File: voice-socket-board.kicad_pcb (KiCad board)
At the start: 2 copper layers, 150 x 100 mm, 278 parts, among them J1 JACK_MONO_SW, J2 JACK_MONO_SW, J3 JACK_MONO_SW, P1 CONN_01X03, P2 CONN_01X03, P3 CONN_02X05, P4 DDR3-DIMM, Q1 MMBT3904, Q2 DMMT3904W, Q3 2N7002, Q4 2N7002, Q5 MMBT3904, Q6 2N3906, Q7 MMBT3904, Q8 MMBT3904, Q9 MMBT3904, SW1 SPST, SW10 SP3T, SW11 SP3T, SW12 SP3T, SW13 SP3T, SW14 SPST, SW15 TACT_SWITCH, SW2 SPST, SW3 SP3T, SW4 SP3T, SW5 SPST, SW6 SPST, SW7 Switch_SPDT_x2, SW8 2P3T, SW9 SP3T, U1 LM833, U10 TL072-, U11 NE5534, U2 TL072-, U3 TL072-, U4 TL072-, U5 TL072-, U6 TL072-, U7 MAX9945, U8 CD4013, U9 TL072-

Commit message: routing. tedious
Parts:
- R119: moved to B.Cu
- moved R119 187.1 mm to (165.5, 121.5), turned to 270 degrees
- moved R73 6.19 mm to (140.5, 127.0), turned to 180 degrees
- moved R115 5.59 mm to (162.5, 127.5), turned to 180 degrees
- moved C61 1.50 mm to (159.5, 121.5)
- moved D8 1.00 mm to (158.0, 121.5)
- moved Q8 1.00 mm to (162.5, 124.5), turned to 180 degrees
- moved R72 0.25 mm to (145.5, 122.5)
- turned R117 to 270 degrees
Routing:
- net EG1_GATE: track 0.00 -> 85.4 mm, vias 0 -> 2
- net Net-(R118-Pad1): track 0.00 -> 21.7 mm
- net Net-(Q3-Pad6): track 0.00 -> 19.4 mm, vias 0 -> 2
- net Net-(D5-Pad1): track 0.00 -> 14.9 mm
- net LFO_GATE: track 17.7 -> 32.3 mm
- net Net-(J3-Pad3): track 0.00 -> 14.4 mm
- net Net-(C20-Pad2): track 3.58 -> 14.7 mm
- net Net-(C21-Pad1): track 4.22 -> 14.4 mm
- net Net-(D5-Pad2): track 0.00 -> 9.41 mm, vias 0 -> 2
- net Net-(C19-Pad1): track 0.00 -> 9.13 mm
- net NOISE: track 0.00 -> 8.63 mm
- net Net-(C20-Pad1): track 0.00 -> 7.63 mm
- net Net-(Q7-Pad2): track 0.00 -> 7.14 mm
- net Net-(D3-Pad2): track 0.00 -> 7.09 mm
- net Net-(C18-Pad1): track 0.00 -> 5.97 mm
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
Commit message: routing..........
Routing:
- net Net-(R97-Pad2): track 0.00 -> 65.1 mm
- net Net-(TR1-Pad1): track 3.59 -> 59.7 mm
- net Net-(R98-Pad2): track 0.00 -> 52.8 mm
- net Net-(C57-Pad2): track 9.72 -> 50.7 mm
- net Net-(R100-Pad2): track 0.00 -> 40.2 mm
- net Net-(C62-Pad2): track 0.00 -> 10.6 mm
- net Net-(C62-Pad1): track 0.00 -> 7.53 mm
- net VCO2_PITCH_CV: track 29.6 -> 35.3 mm
- net KEY_TRACK: track 17.2 -> 20.7 mm
- net Net-(J2-Pad3): track 0.00 -> 2.00 mm
- net +12V: track 175.8 -> 177.1 mm
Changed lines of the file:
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@@
   (general
     (links 783)
-    (no_connects 404)
+    (no_connects 385)
     (area 26.770899 -11.00852 196.421058 140.8282)
     (thickness 1.6)
     (drawings 19)
-    (tracks 909)
+    (tracks 977)
     (zones 0)
     (modules 278)
@@
   (segment (start 121 97.172183) (end 121 94.15) (width 0.254) (layer B.Cu) (net 29))
   (segment (start 127.3509 102.25) (end 129.1491 102.25) (width 0.6096) (layer B.Cu) (net 30))
+  (segment (start 159.6009 136) (end 160.8991 136) (width 0.3048) (layer B.Cu) (net 31))
   (segment (start 114.606 126.0319) (end 111.264818 126.0319) (width 0.3048) (layer B.Cu) (net 31))
   (segment (start 111.264818 126.0319) (end 110.927101 125.694183) (width 0.3048) (layer B.Cu) (net 31))
@@
   (segment (start 119.5 84.3509) (end 121.25 84.3509) (width 0.254) (layer B.Cu) (net 38))
   (segment (start 115.5 90.3509) (end 115.3349 90.3509) (width 0.254) (layer B.Cu) (net 38))
+  (segment (start 114.5 82.75) (end 121.1 82.75) (width 0.254) (layer F.Cu) (net 39))
+  (segment (start 121.1 82.75) (end 128.7 90.35) (width 0.254) (layer F.Cu) (net 39))
+  (segment (start 132.864418 90.35) (end 139.6 90.35) (width 0.254) (layer F.Cu) (net 39))
+  (segment (start 128.7 90.35) (end 131.635582 90.35) (width 0.254) (layer F.Cu) (net 39))
+  (segment (start 132.664418 90.15) (end 132.864418 90.35) (width 0.254) (layer F.Cu) (net 39))
+  (segment (start 131.635582 90.35) (end 131.835582 90.15) (width 0.254) (layer F.Cu) (net 39))
+  (segment (start 131.835582 90.15) (end 132.664418 90.15) (width 0.254) (layer F.Cu) (net 39))
+  (segment (start 139.6 90.35) (end 143.49 86.46) (width 0.254) (layer F.Cu) (net 39))
+  (segment (start 145.742765 86.46) (end 147 86.46) (width 0.254) (layer F.Cu) (net 39))
+  (segment (start 143.49 86.46) (end 145.742765 86.46) (width 0.254) (layer F.Cu) (net 39))
+  (segment (start 147 86.46) (end 147.888999 87.348999) (width 0.254) (layer F.Cu) (net 39))
+  (segment (start 147.888999 87.348999) (end 149.54 89) (width 0.254) (layer F.Cu) (net 39))
   (segment (start 117.5 88.6491) (end 115.75 88.6491) (width 0.254) (layer B.Cu) (net 39))
   (segment (start 115.75 88.6491) (end 115.75 86.0868) (width 0.254) (layer B.Cu) (net 39))
@@
   (segment (start 80.3991 134.86566) (end 82.98976 132.275) (width 0.254) (layer B.Cu) (net 57))
   (segment (start 82.98976 132.275) (end 83.894 132.275) (width 0.254) (layer B.Cu) (net 57))
+  (segment (start 187.5 123.6009) (end 187.5 125.6) (width 0.254) (layer B.Cu) (net 59))
   (segment (start 163.3509 127.5) (end 164.0113 127.5) (width 0.254) (layer B.Cu) (net 61))
   (segment (start 164.0113 127.5) (end 171.9113 135.4) (width 0.254) (layer B.Cu) (net 61))
@@
   (segment (start 98.5 91.8509) (end 98.5 92.7) (width 0.254) (layer B.Cu) (net 88))
   (segment (start 98.5 91.8509) (end 96.75 91.8509) (width 0.254) (layer B.Cu) (net 88))
+  (segment (start 104 99.85) (end 104 101.6491) (width 0.254) (layer B.Cu) (net 89))
+  (segment (start 104 101.6491) (end 104.25 101.8991) (width 0.254) (layer B.Cu) (net 89))
+  (segment (start 106 101.8991) (end 104.25 101.8991) (width 0.254) (layer B.Cu) (net 89))
+  (segment (start 102.5 101.8991) (end 104.25 101.8991) (width 0.254) (layer B.Cu) (net 89))
   (segment (start 99 85.3509) (end 102.6091 85.3509) (width 0.254) (layer B.Cu) (net 89))
   (segment (start 102.6091 85.3509) (end 102.75 85.21) (width 0.254) (layer B.Cu) (net 89))
@@
   (segment (start 79.6013 132.91) (end 79.21024 132.91) (width 0.254) (layer B.Cu) (net 137))
   (segment (start 79.21024 132.91) (end 78.306 132.91) (width 0.254) (layer B.Cu) (net 137))
+  (segment (start 146.75 55.7) (end 147.81066 55.7) (width 0.254) (layer B.Cu) (net 138))
+  (segment (start 147.81066 55.7) (end 150.25 55.7) (width 0.254) (layer B.Cu) (net 138))
   (segment (start 77.25 129.1491) (end 77.25 125.75) (width 0.254) (layer B.Cu) (net 138))
   (segment (start 77.25 125.75) (end 77.5 125.5) (width 0.254) (layer B.Cu) (net 138))
@@
   (segment (start 124.555638 66.5) (end 125.45 66.5) (width 0.254) (layer B.Cu) (net 159))
   (segment (start 128.75 131.7) (end 132.25 131.7) (width 0.254) (layer B.Cu) (net 162))
+  (segment (start 124.75 82.6491) (end 124.75 81.85) (width 0.254) (layer B.Cu) (net 169))
+  (segment (start 124.75 81.85) (end 125.292789 81.307211) (width 0.254) (layer B.Cu) (net 169))
+  (segment (start 125.292789 81.307211) (end 135.842789 81.307211) (width 0.254) (layer B.Cu) (net 169))
+  (segment (start 135.842789 81.307211) (end 138.7 78.45) (width 0.254) (layer B.Cu) (net 169))
+  (segment (start 138.7 71.55) (end 141.3 68.95) (width 0.254) (layer B.Cu) (net 169))
+  (segment (start 138.7 78.45) (end 138.7 71.55) (width 0.254) (layer B.Cu) (net 169))
+  (segment (start 141.3 68.95) (end 162.05 68.95) (width 0.254) (layer B.Cu) (net 169))
+  (segment (start 162.05 68.95) (end 173.625001 57.374999) (width 0.254) (layer B.Cu) (net 169))
+  (segment (start 173.625001 57.374999) (end 174.5 56.5) (width 0.254) (layer B.Cu) (net 169))
+  (segment (start 124.2 80.85) (end 134.8 80.85) (width 0.254) (layer B.Cu) (net 170))
+  (segment (start 142 53.25) (end 144.55 50.7) (width 0.254) (layer B.Cu) (net 170))
+  (segment (start 134.8 80.85) (end 137.7 77.95) (width 0.254) (layer B.Cu) (net 170))
+  (segment (start 123 82.6491) (end 123 82.05) (width 0.254) (layer B.Cu) (net 170))
+  (segment (start 123 82.05) (end 124.2 80.85) (width 0.254) (layer B.Cu) (net 170))
+  (segment (start 137.7 71.15) (end 142 66.85) (width 0.254) (layer B.Cu) (net 170))
+  (segment (start 137.7 77.95) (end 137.7 71.15) (width 0.254) (layer B.Cu) (net 170))
+  (segment (start 142 66.85) (end 142 53.25) (width 0.254) (layer B.Cu) (net 170))
+  (segment (start 144.55 50.7) (end 146.75 50.7) (width 0.254) (layer B.Cu) (net 170))
+  (segment (start 146.75 50.7) (end 150.25 50.7) (width 0.254) (layer B.Cu) (net 170))
   (segment (start 117.5 56.5) (end 117.5 57.737436) (width 0.254) (layer B.Cu) (net 171))
   (segment (start 117.5 57.737436) (end 113.5 61.737436) (width 0.254) (layer B.Cu) (net 171))
@@
   (segment (start 118.75 81.2387) (end 119.5 81.9887) (width 0.254) (layer B.Cu) (net 171))
   (segment (start 119.5 81.9887) (end 119.5 82.6491) (width 0.254) (layer B.Cu) (net 171))
+  (segment (start 130.5 56.5) (end 136.1 62.1) (width 0.254) (layer B.Cu) (net 172))
+  (segment (start 136.1 62.1) (end 136.1 76.314836) (width 0.254) (layer B.Cu) (net 172))
+  (segment (start 136.1 76.314836) (end 134.914836 77.5) (width 0.254) (layer B.Cu) (net 172))
+  (segment (start 134.914836 77.5) (end 125.35 77.5) (width 0.254) (layer B.Cu) (net 172))
+  (segment (start 125.35 77.5) (end 121.25 81.6) (width 0.254) (layer B.Cu) (net 172))
+  (segment (start 121.25 81.6) (end 121.25 82.6491) (width 0.254) (layer B.Cu) (net 172))
   (segment (start 134.79 89) (end 134.79 88.51) (width 0.254) (layer B.Cu) (net 174))
   (segment (start 134.79 88.51) (end 135.8 87.5) (width 0.254) (layer B.Cu) (net 174))
@@
   (segment (start 60.3 74.2) (end 55 79.5) (width 0.254) (layer B.Cu) (net 188))
   (segment (start 67.25 74.2) (end 63.75 74.2) (width 0.254) (layer B.Cu) (net 188))
+  (segment (start 129.71 89) (end 130.598999 88.111001) (width 0.254) (layer F.Cu) (net 189))
+  (segment (start 130.598999 85.301001) (end 137.5 78.4) (width 0.254) (layer F.Cu) (net 189))
+  (segment (start 130.598999 88.111001) (end 130.598999 85.301001) (width 0.254) (layer F.Cu) (net 189))
+  (segment (start 137.5 78.4) (end 137.5 64.15) (width 0.254) (layer F.Cu) (net 189))
+  (segment (start 137.5 64.15) (end 142.3 59.35) (width 0.254) (layer F.Cu) (net 189))
+  (segment (start 142.3 59.35) (end 160.1 59.35) (width 0.254) (layer F.Cu) (net 189))
+  (segment (start 160.1 59.35) (end 161.5 57.95) (width 0.254) (layer F.Cu) (net 189))
+  (segment (start 161.5 57.95) (end 161.5 56.5) (width 0.254) (layer F.Cu) (net 189))
   (segment (start 132.25 91.54) (end 129.71 89) (width 0.254) (layer B.Cu) (net 189))
   (segment (start 119.55 65.85) (end 120.529 65.85) (width 0.254) (layer B.Cu) (net 190))
@@
   (segment (start 126.505201 67.073799) (end 126.429 67.15) (width 0.254) (layer B.Cu) (net 191))
   (segment (start 126.429 67.15) (end 125.45 67.15) (width 0.254) (layer B.Cu) (net 191))
+  (segment (start 181.1491 127.25) (end 181.1491 125.5) (width 0.254) (layer B.Cu) (net 192))
+  (segment (start 179.8509 125.5) (end 181.1491 125.5) (width 0.254) (layer B.Cu) (net 192))
+  (segment (start 179.3 122.385) (end 180.329 122.385) (width 0.254) (layer B.Cu) (net 192))
+  (segment (start 180.329 122.385) (end 181.1491 123.2051) (width 0.254) (layer B.Cu) (net 192))
+  (segment (start 181.1491 123.2051) (end 181.1491 124.6745) (width 0.254) (layer B.Cu) (net 192))
+  (segment (start 181.1491 124.6745) (end 181.1491 125.5) (width 0.254) (layer B.Cu) (net 192))
+  (segment (start 186.514 121.9) (end 186.5149 121.8991) (width 0.254) (layer B.Cu) (net 193))
+  (segment (start 186.5149 121.8991) (end 187.5 121.8991) (width 0.254) (layer B.Cu) (net 193))
+  (segment (start 184.7 121.115) (end 185.729 121.115) (width 0.254) (layer B.Cu) (net 193))
+  (segment (start 185.729 121.115) (end 186.514 121.9) (width 0.254) (layer B.Cu) (net 193))
+  (segment (start 184.7 121.115) (end 183.785 121.115) (width 0.254) (layer B.Cu) (net 193))
+  (segment (start 183.785 121.115) (end 182.8509 122.0491) (width 0.254) (layer B.Cu) (net 193))
+  (segment (start 182.8509 122.0491) (end 182.8509 124.6745) (width 0.254) (layer B.Cu) (net 193))
+  (segment (start 182.8509 124.6745) (end 182.8509 125.5) (width 0.254) (layer B.Cu) (net 193))
+  (segment (start 182.8509 127.25) (end 182.8509 125.5) (width 0.254) (layer B.Cu) (net 193))
 )

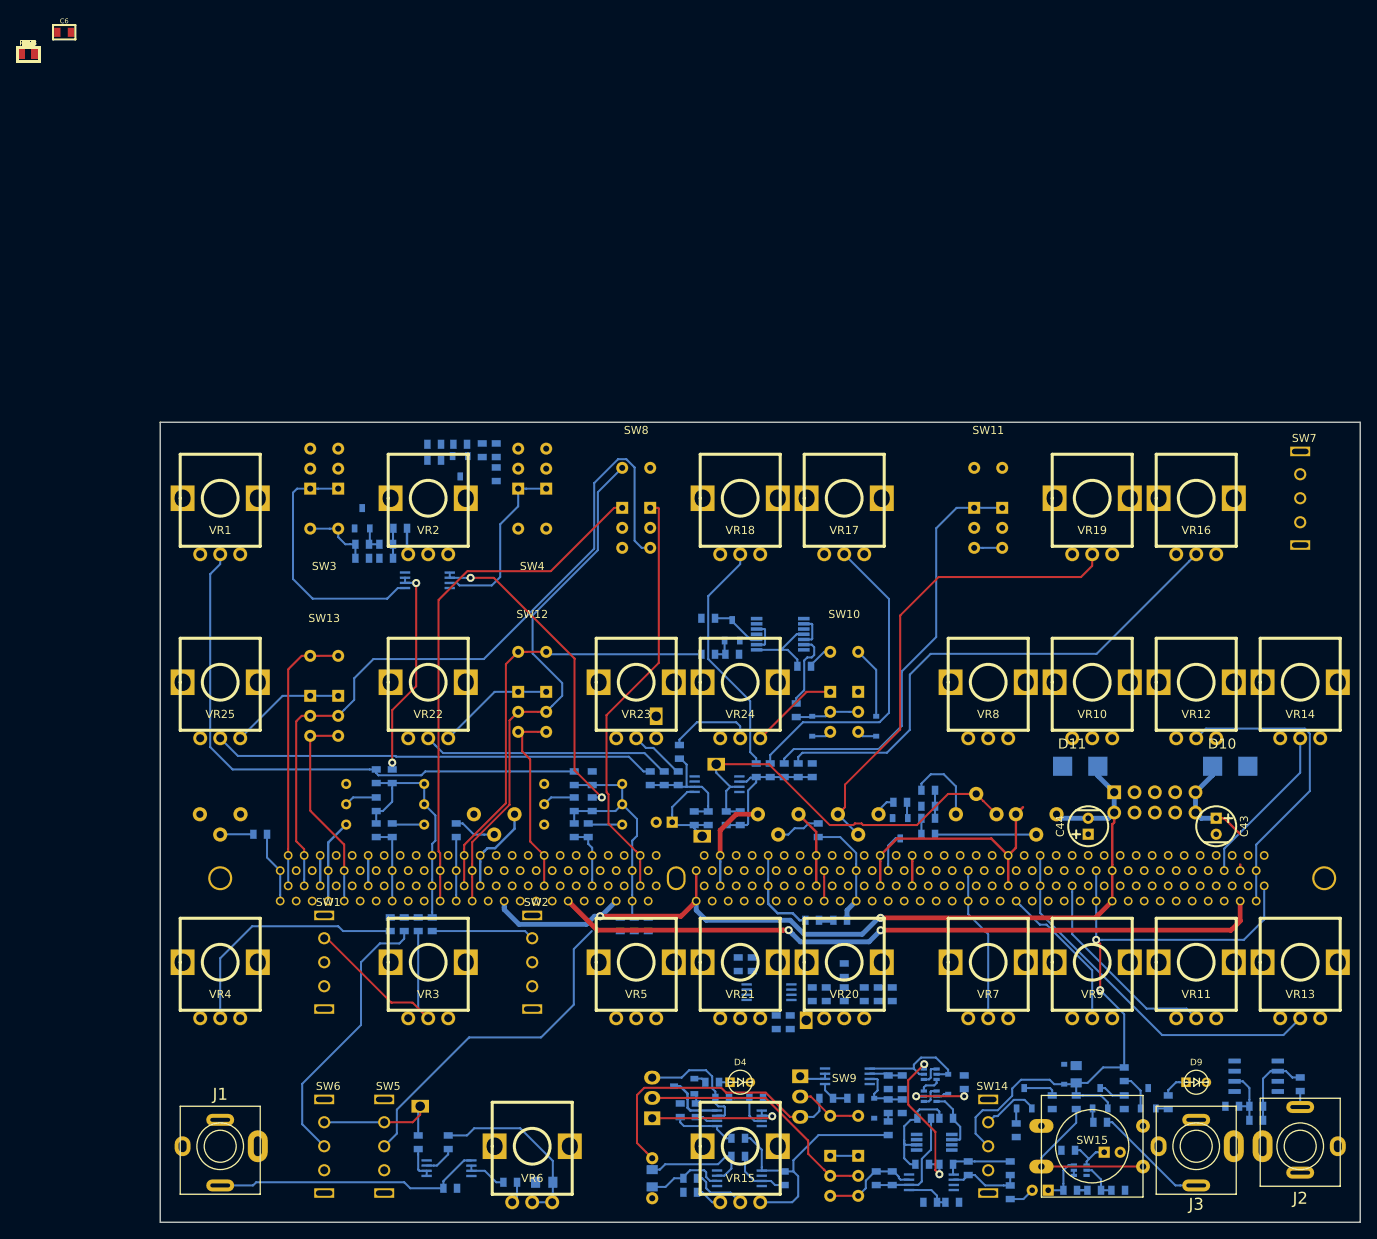
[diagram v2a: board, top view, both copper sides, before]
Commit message: routing. added VCA CTRL from EG1. duh. forgot it in schematic
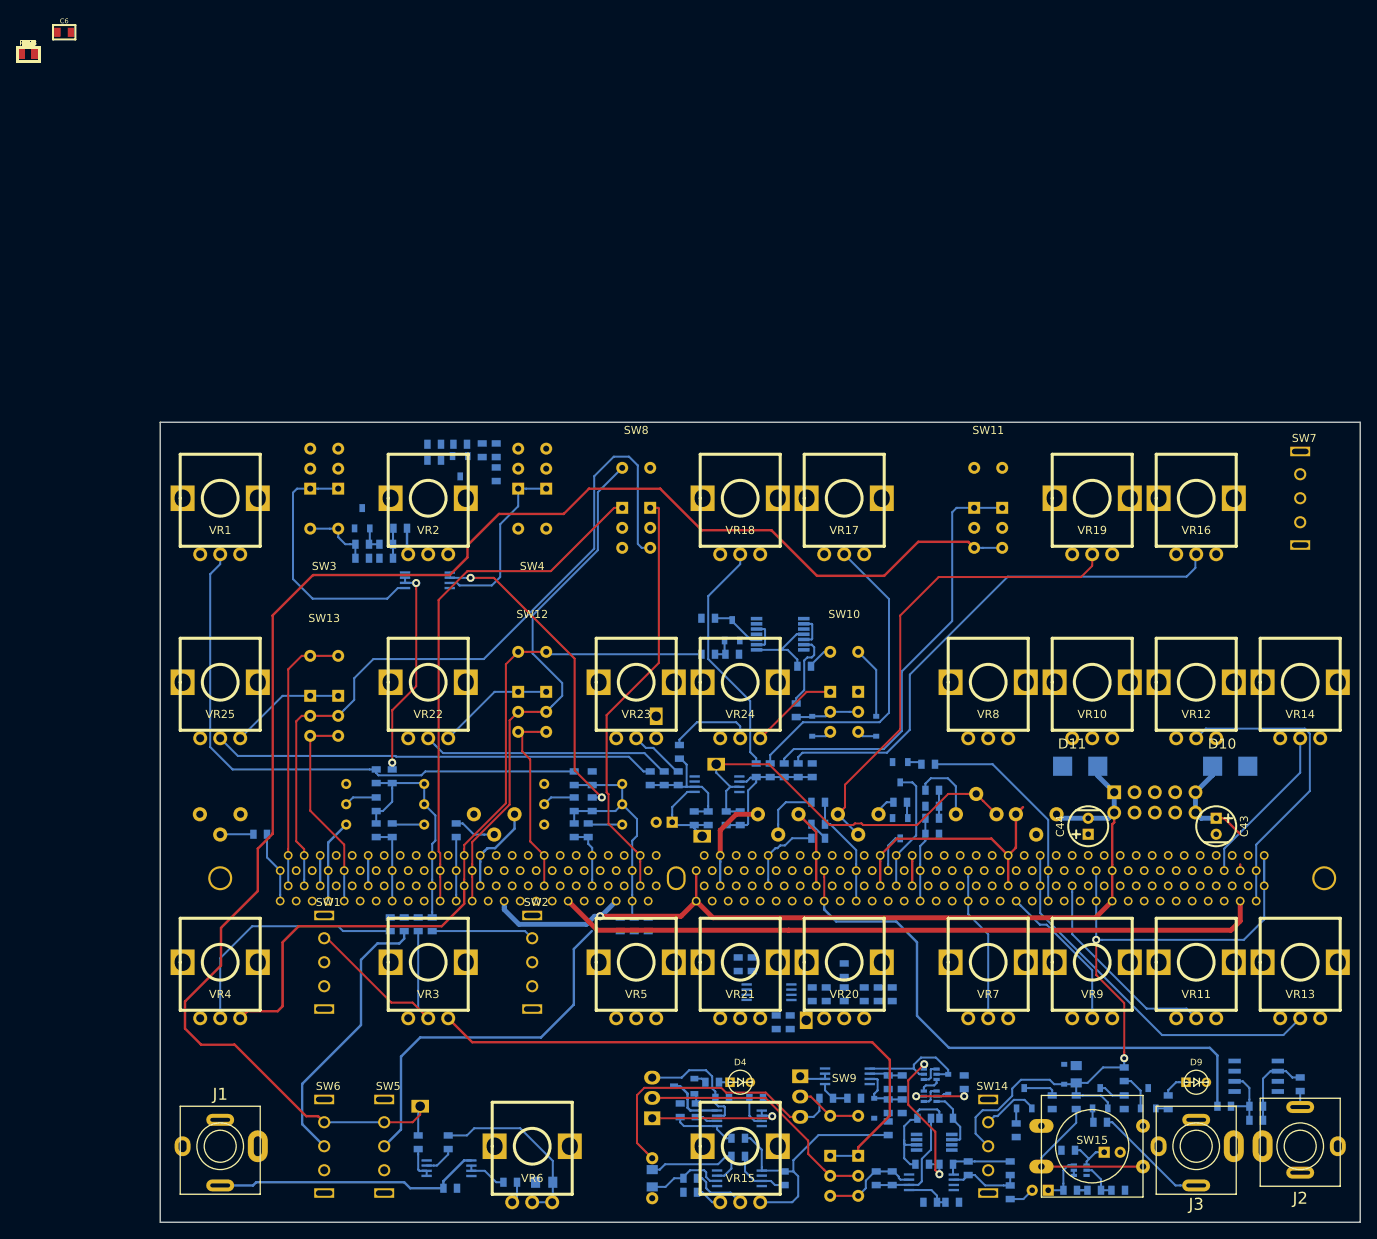
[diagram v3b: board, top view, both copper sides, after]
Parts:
- added Q10: 2N3906, MyModules:SOT23-JRL, B.Cu at (137.5, 83.8)
- added R124: 27K, MyModules:SM0603-R-JRL, B.Cu at (141.0, 82.8)
- moved R77 12.3 mm to (127.2, 90.2)
- moved C22 10.3 mm to (127.2, 92.0)
- moved R78 3.50 mm to (127.2, 87.5), turned to 0 degrees
- moved R121 1.00 mm to (178.0, 125.5)
- moved C58 0.50 mm to (141.5, 88.0)
- moved R106 0.50 mm to (141.5, 86.0)
- moved R107 0.50 mm to (141.5, 91.5)
- moved R108 0.50 mm to (141.5, 89.5)
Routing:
- net KEY_TRACK: track 20.7 -> 200.9 mm
- net LFO_OUT: track 3.50 -> 74.5 mm
- net VCA_OUT: track 3.80 -> 73.3 mm
- net VCO2_SAW: track 55.1 -> 95.9 mm
- net EG1_ENV_OUT: track 0.00 -> 27.2 mm
- net VCA_CTRL: track 0.00 -> 15.7 mm
- net Net-(R107-Pad2): track 12.7 -> 0.06 mm
- net VCF_CTRL: track 2.00 -> 10.6 mm
- net EG1_GATE: track 85.4 -> 89.2 mm
- net VCO2_GLIDE_CV: track 42.9 -> 46.5 mm
- net -12V: track 142.7 -> 140.3 mm, vias 2 -> 1
- net Net-(R78-Pad1): track 5.58 -> 7.63 mm
- net Net-(Q10-Pad1): track 0.00 -> 1.81 mm
- net VCF_OUT: track 11.5 -> 10.1 mm
- net +12V: track 177.1 -> 175.9 mm, vias 2 -> 0
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
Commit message: more routing. need to rearrange power connector, main rail filter caps and protection diodes
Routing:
- net LFO_OUT: track 74.5 -> 232.8 mm, vias 0 -> 1
- net EG2_OUT: track 0.00 -> 59.5 mm
- net +12V: track 175.9 -> 199.8 mm, vias 0 -> 1
- net EG2_ENV_MOD: track 12.9 -> 34.4 mm
- net -12V: track 140.3 -> 123.4 mm
- net KEY_TRACK: track 200.9 -> 198.1 mm
- net VCO2_SAW: track 95.9 -> 93.7 mm
- net Net-(R6-Pad2): track 30.7 -> 31.2 mm
